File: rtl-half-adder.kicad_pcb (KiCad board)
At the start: 2 copper layers, 152.4 x 114.3 mm, 78 parts, among them Q1 Q_NPN_EBC, Q10 Q_NPN_EBC, Q11 Q_NPN_EBC, Q12 Q_NPN_EBC, Q13 Q_NPN_EBC, Q14 Q_NPN_BEC, Q15 Q_NPN_BEC, Q16 Q_NPN_EBC, Q17 Q_NPN_BEC, Q18 Q_NPN_BEC, Q19 Q_NPN_EBC, Q2 Q_NPN_EBC, Q3 Q_NPN_EBC, Q4 Q_NPN_EBC, Q5 Q_NPN_EBC, Q6 Q_NPN_EBC, Q7 Q_NPN_EBC, Q8 Q_NPN_EBC, Q9 Q_NPN_EBC, SW1 SW_DIP_x02

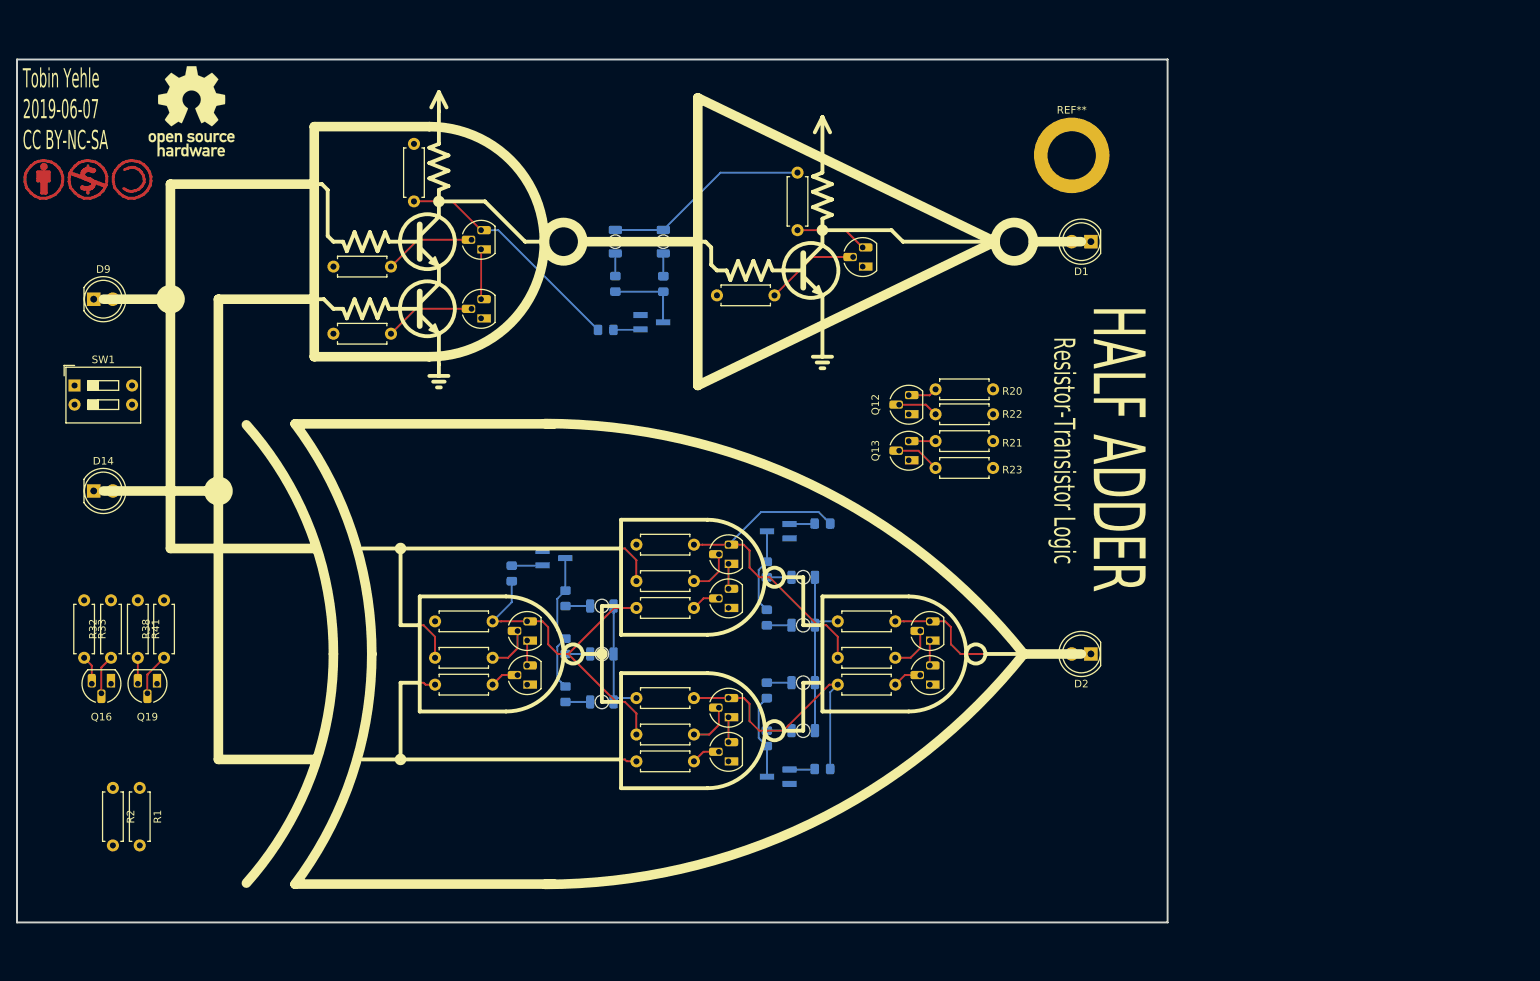
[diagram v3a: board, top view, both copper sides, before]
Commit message: refactor numeric assignments
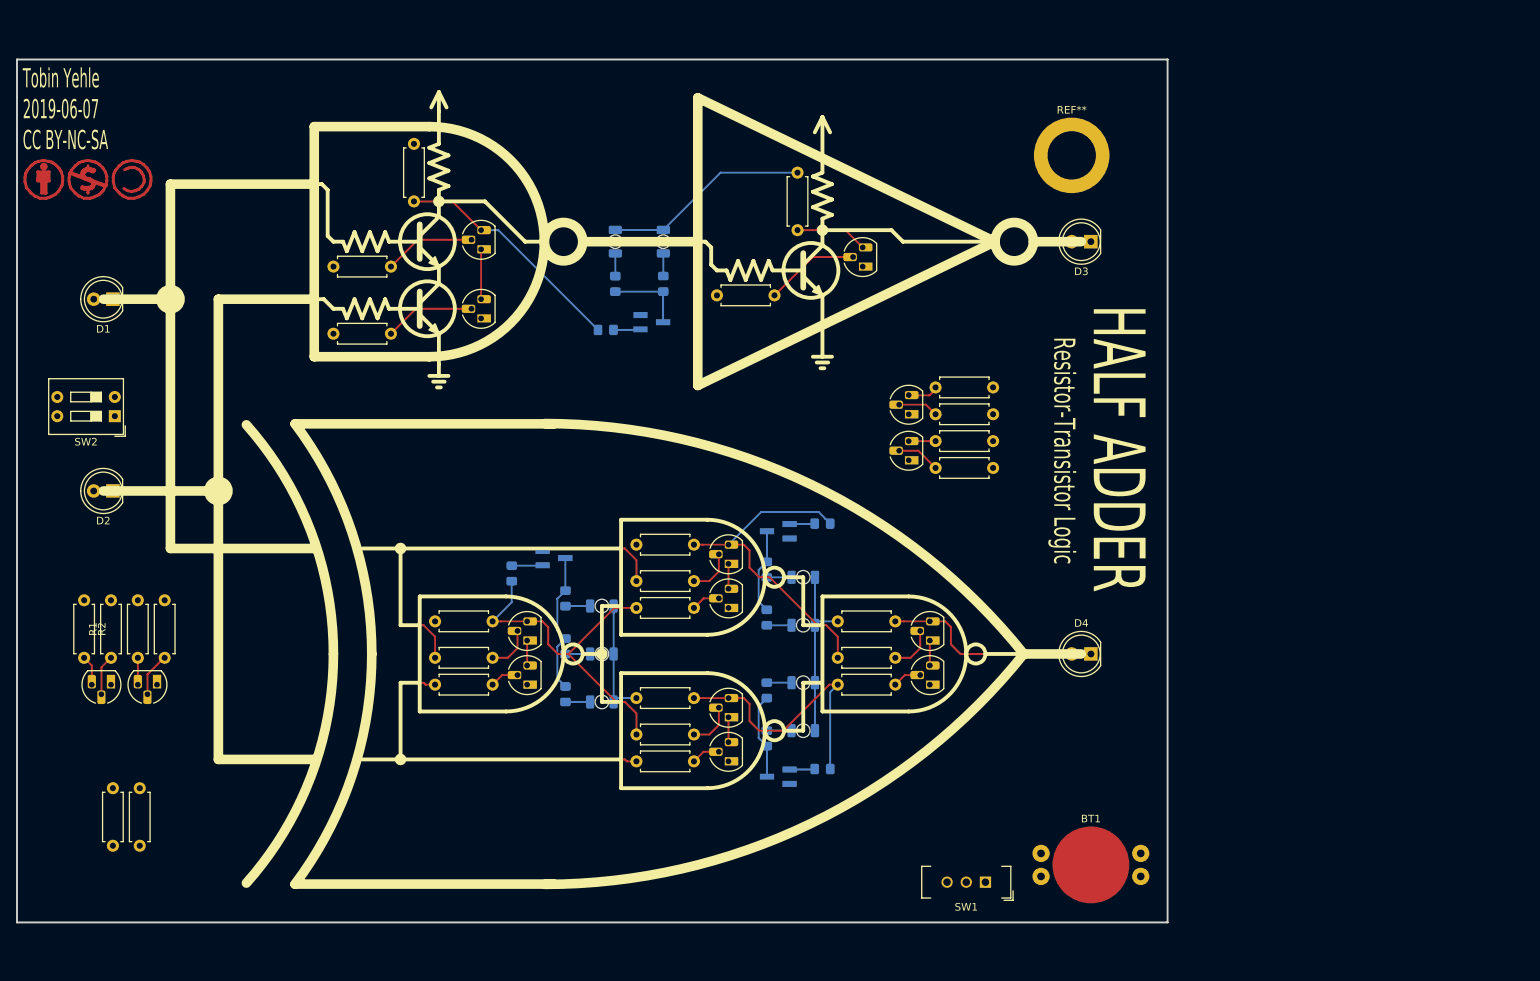
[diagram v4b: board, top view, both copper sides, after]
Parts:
- removed D14: LED, LED_THT:LED_D5.0mm
- removed D15: LED, --Project:LED_1206_3216Metric_ReverseMount_Hole1.8x2.4mm
- removed R41: 68, Resistor_THT:R_Axial_DIN0207_L6.3mm_D2.5mm_P7.62mm_Horizontal
- removed R42: 68, Resistor_SMD:R_0805_2012Metric_Pad1.15x1.40mm_HandSolder
- removed the REF** at (73.9, 45.0)
- added BT1: Battery_Cell, --Project:BatteryHolder_CR1220_THT, F.Cu at (193.0, 144.8)
- added D7: LED, --Project:LED_1206_3216Metric_ReverseMount_Hole1.8x2.4mm, B.Cu at (128.3, 110.5)
- added D8: LED, --Project:LED_1206_3216Metric_ReverseMount_Hole1.8x2.4mm, B.Cu at (128.3, 116.8)
- added R30: 68, Resistor_SMD:R_0805_2012Metric_Pad1.15x1.40mm_HandSolder, B.Cu at (136.4, 67.8)
- added R31: 10k, Resistor_SMD:R_0805_2012Metric_Pad1.15x1.40mm_HandSolder, B.Cu at (116.3, 106.2)
- added SW2: SW_DIP_x02, Button_Switch_THT:SW_DIP_SPSTx02_Slide_9.78x7.26mm_W7.62mm_P2.54mm, F.Cu at (63.8, 85.3)
- D3, D4: footprint --Project:LED_1206_3216Metric_ReverseMount_Hole1.8x2.4mm -> LED_THT:LED_D5.0mm; moved to F.Cu
- D9: footprint LED_THT:LED_D5.0mm -> --Project:LED_1206_3216Metric_ReverseMount_Hole1.8x2.4mm; moved to B.Cu
- Q14, Q15: value Q_NPN_BEC -> Q_NPN_EBC; footprint Package_TO_SOT_SMD:SOT-23_Handsoldering -> Package_TO_SOT_THT:TO-92_HandSolder; moved to F.Cu
- Q16, Q19: value Q_NPN_EBC -> Q_NPN_BEC; footprint Package_TO_SOT_THT:TO-92_HandSolder -> Package_TO_SOT_SMD:SOT-23_Handsoldering; moved to B.Cu
- R12, R17, R18, R23, R9: value 10k -> 1k
- R14, R15, R16, R19, R7, R8: value 1k -> 10k
- R2, R34, R4: value 10k -> 68
- R20: value 68 -> 1k
- R21, R28: value 68 -> 10k
- R24, R25, R26, R27: footprint Resistor_SMD:R_0805_2012Metric_Pad1.15x1.40mm_HandSolder -> Resistor_THT:R_Axial_DIN0207_L6.3mm_D2.5mm_P7.62mm_Horizontal; moved to F.Cu
- R32: value 10k -> 68; footprint Resistor_THT:R_Axial_DIN0207_L6.3mm_D2.5mm_P7.62mm_Horizontal -> Resistor_SMD:R_0805_2012Metric_Pad1.15x1.40mm_HandSolder; moved to B.Cu
- R33, R38: footprint Resistor_THT:R_Axial_DIN0207_L6.3mm_D2.5mm_P7.62mm_Horizontal -> Resistor_SMD:R_0805_2012Metric_Pad1.15x1.40mm_HandSolder; moved to B.Cu
- SW1: value SW_DIP_x02 -> SW_SPDT; footprint Button_Switch_THT:SW_DIP_SPSTx02_Slide_9.78x7.26mm_W7.62mm_P2.54mm -> --Project:SW_EG1218_SPDT
- moved SW1 135.2 mm to (176.5, 147.1), turned to 180 degrees
- moved D2 131.3 mm to (63.5, 95.2)
- moved D1 129.8 mm to (63.5, 69.8)
- moved R38 88.4 mm to (157.5, 132.1), turned to 0 degrees
- moved R12 86.6 mm to (103.4, 49.3), turned to 270 degrees
- moved Q16 86.2 mm to (134.9, 72.9), turned to 0 degrees
- moved D9 85.9 mm to (128.3, 123.2)
- moved Q19 83.2 mm to (151.6, 133.1)
- moved Q1 75.7 mm to (63.2, 120.9), turned to 180 degrees
- moved R7 68.9 mm to (113.8, 117.3), turned to 180 degrees
- moved Q2 64.8 mm to (69.3, 120.9), turned to 180 degrees
- moved R33 64.0 mm to (123.4, 115.8), turned to 90 degrees
- moved D3 63.0 mm to (193.0, 62.2), turned to 180 degrees
- moved R9 62.3 mm to (106.2, 112.5), turned to 0 degrees
- moved R32 60.7 mm to (123.4, 109.5)
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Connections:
- Q1 pad 1: Net-(Q1-Pad1) -> GND
- Q1 pad 3: NAND1 -> /A_GATE
- Q10 pad 1: Net-(Q10-Pad1) -> GND
- Q10 pad 3: SUM -> Net-(Q10-Pad3)
- Q11 pad 3: Net-(Q10-Pad1) -> CARRY
- Q12 pad 1: GND -> Net-(Q12-Pad1)
- Q12 pad 3: Net-(Q12-Pad3) -> SUM
- Q13 pad 3: Net-(Q13-Pad3) -> Net-(Q12-Pad1)
- Q14 pad 1: Net-(Q14-Pad1) -> GND
- Q14 pad 2: GND -> Net-(Q14-Pad2)
- Q14 pad 3: Net-(Q14-Pad3) -> /CARRY_GATE
- Q15 pad 1: Net-(Q15-Pad1) -> GND
- Q15 pad 2: GND -> Net-(Q15-Pad2)
- Q15 pad 3: Net-(Q15-Pad3) -> /SUM_GATE
- Q16 pad 1: GND -> Net-(Q16-Pad1)
- Q16 pad 2: Net-(Q16-Pad2) -> GND
- Q19 pad 1: GND -> Net-(Q19-Pad1)
- Q19 pad 2: Net-(Q19-Pad2) -> GND
- Q2 pad 3: Net-(Q1-Pad1) -> /B_GATE
- Q5 pad 1: GND -> Net-(Q5-Pad1)
- Q5 pad 3: CARRY -> NAND1
- Q6 pad 1: Net-(Q6-Pad1) -> GND
- Q6 pad 3: XOR2 -> Net-(Q5-Pad1)
- Q7 pad 1: GND -> Net-(Q7-Pad1)
- Q7 pad 3: Net-(Q6-Pad1) -> XOR2
- Q8 pad 1: Net-(Q8-Pad1) -> GND
- Q8 pad 3: XOR3 -> Net-(Q7-Pad1)
- Q9 pad 1: GND -> Net-(Q10-Pad3)
- Q9 pad 3: Net-(Q8-Pad1) -> XOR3
- R1 pad 1: B -> Net-(Q1-Pad2)
- R1 pad 2: GND -> A
- R10 pad 1: Net-(Q6-Pad2) -> Net-(Q5-Pad2)
- R11 pad 1: Net-(Q7-Pad2) -> Net-(Q6-Pad2)
- R11 pad 2: XOR1 -> B
- R12 pad 1: Net-(Q8-Pad2) -> VCC
- R12 pad 2: XOR1 -> NAND1
- R13 pad 1: Net-(Q9-Pad2) -> Net-(Q7-Pad2)
- R13 pad 2: B -> A
- R14 pad 1: VCC -> Net-(Q8-Pad2)
- R14 pad 2: CARRY -> XOR1
- R15 pad 1: VCC -> Net-(Q9-Pad2)
- R15 pad 2: XOR2 -> XOR1
- R16 pad 1: VCC -> Net-(Q10-Pad2)
- R16 pad 2: XOR3 -> B
- R17 pad 1: Net-(Q10-Pad2) -> VCC
- R18 pad 1: Net-(Q11-Pad2) -> VCC
- R19 pad 1: VCC -> Net-(Q11-Pad2)
- R19 pad 2: SUM -> NAND1
- R2 pad 1: A -> Net-(D1-Pad1)
- R2 pad 2: GND -> /A_GATE
- R20 pad 1: Net-(D1-Pad1) -> VCC
- R20 pad 2: Net-(Q12-Pad3) -> CARRY
- R21 pad 1: Net-(D2-Pad1) -> Net-(Q12-Pad2)
- R21 pad 2: Net-(Q13-Pad3) -> XOR2
- R22 pad 1: Net-(Q12-Pad2) -> Net-(Q13-Pad2)
- R22 pad 2: CARRY -> XOR3
- R23 pad 1: Net-(Q13-Pad2) -> VCC
- R24 pad 1: Net-(Q14-Pad1) -> Net-(Q14-Pad2)
- R24 pad 2: NAND1 -> CARRY
- R25 pad 1: Net-(Q15-Pad1) -> Net-(Q15-Pad2)
- R25 pad 2: XOR2 -> SUM
- R26 pad 2: Net-(Q14-Pad3) -> /CARRY_GATE
- R27 pad 2: Net-(Q15-Pad3) -> /SUM_GATE
- R28 pad 1: Net-(D5-Pad1) -> Net-(Q16-Pad1)
- R28 pad 2: Net-(Q14-Pad3) -> NAND1
- R29 pad 1: Net-(D6-Pad1) -> Net-(D5-Pad1)
- R29 pad 2: Net-(Q15-Pad3) -> Net-(Q16-Pad3)
- R3 pad 1: Net-(Q1-Pad2) -> Net-(Q2-Pad2)
- R3 pad 2: A -> B
- R32 pad 1: Net-(Q16-Pad2) -> Net-(D7-Pad1)
- R32 pad 2: A -> Net-(Q17-Pad3)
- R33 pad 1: Net-(D9-Pad1) -> Net-(D8-Pad1)
- R33 pad 2: Net-(Q16-Pad3) -> Net-(Q17-Pad3)
- R34 pad 1: Net-(Q17-Pad1) -> Net-(D9-Pad1)
- R34 pad 2: XOR1 -> Net-(Q17-Pad3)
- R35 pad 2: XOR3 -> XOR2
- R36 pad 2: Net-(Q17-Pad3) -> Net-(Q18-Pad3)
- R38 pad 1: Net-(Q19-Pad2) -> Net-(Q19-Pad1)
- R38 pad 2: B -> XOR3
- R39 pad 2: Net-(Q17-Pad3) -> Net-(Q19-Pad3)
- R4 pad 1: Net-(Q2-Pad2) -> Net-(D2-Pad1)
- R4 pad 2: B -> /B_GATE
- R40 pad 2: Net-(Q18-Pad3) -> Net-(Q19-Pad3)
- R5 pad 1: Net-(Q3-Pad2) -> B
- R5 pad 2: A -> GND
- R6 pad 1: Net-(Q4-Pad2) -> A
- R6 pad 2: B -> GND
- R7 pad 1: VCC -> Net-(Q3-Pad2)
- R7 pad 2: NAND1 -> A
- R8 pad 1: VCC -> Net-(Q4-Pad2)
- R8 pad 2: XOR1 -> B
- R9 pad 1: Net-(Q5-Pad2) -> VCC
- R9 pad 2: NAND1 -> XOR1
- SW1 pad 1: VCC -> Net-(BT1-Pad1)
- SW1 pad 3: B -> (no net)
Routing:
- net Net-(Q15-Pad3): track 11.3 -> 0.00 mm
- net Net-(Q14-Pad3): track 10.4 -> 0.00 mm
- net Net-(Q11-Pad2): track 3.83 -> 12.5 mm
- net Net-(Q19-Pad3): track 3.43 -> 11.3 mm
- net Net-(Q1-Pad2): track 12.1 -> 5.35 mm
- net Net-(Q5-Pad1): track 0.00 -> 6.60 mm
- net Net-(Q1-Pad1): track 6.60 -> 0.00 mm
- net Net-(Q16-Pad3): track 3.85 -> 10.4 mm
- net Net-(Q2-Pad2): track 12.0 -> 5.61 mm
- net Net-(Q6-Pad2): track 6.11 -> 12.0 mm
- net Net-(Q15-Pad2): track 0.00 -> 5.77 mm
- net Net-(Q19-Pad2): track 5.61 -> 0.00 mm
- net Net-(Q14-Pad2): track 0.00 -> 5.35 mm
- net Net-(Q16-Pad2): track 5.23 -> 0.00 mm
- net Net-(Q12-Pad3): track 3.90 -> 0.00 mm
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
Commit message: fix front fab layer
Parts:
- added SW3: SW_SPDT, --Project:SW_EG1218_SPDT, F.Cu at (61.0, 85.9)
- REF**: value MountingHole_6.4mm_M6_ISO14580_Pad -> MountingHole_6.4mm
- SW2: value SW_DIP_x02 -> SW_SPDT; footprint Button_Switch_THT:SW_DIP_SPSTx02_Slide_9.78x7.26mm_W7.62mm_P2.54mm -> --Project:SW_EG1218_SPDT
- moved SW2 6.71 mm to (61.0, 79.2)
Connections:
- SW1 pad 3: (no net) -> Net-(SW1-Pad3)
- SW2 pad 1: VCC -> A
- SW2 pad 3: B -> Net-(SW2-Pad3)
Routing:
- net VCC: track 66.8 -> 391.5 mm
- net A: track 41.1 -> 212.0 mm, vias 0 -> 2
- net B: track 34.5 -> 159.2 mm
- net Net-(D1-Pad1): track 0.00 -> 47.8 mm
- net Net-(BT1-Pad1): track 0.00 -> 40.2 mm
- net NAND1: track 31.4 -> 66.2 mm
- net CARRY: track 9.58 -> 44.2 mm
- net Net-(D4-Pad1): track 0.00 -> 33.6 mm
- net Net-(D3-Pad1): track 0.00 -> 24.7 mm
- net Net-(D2-Pad1): track 0.00 -> 15.8 mm
- net SUM: track 21.4 -> 30.3 mm
- added copper zone on B.Cu, net GND
- added copper zone on F.Cu, net GND

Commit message: put notes on the back
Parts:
- added REF**: OSHW-Logo_11.4x12mm_SilkScreen, Symbol:OSHW-Logo_11.4x12mm_SilkScreen, B.Cu at (139.4, 46.0)
- REF** (x3): moved to B.Cu
- moved REF** 109.4 mm to (163.6, 47.9), turned to 180 degrees
- moved REF** 97.7 mm to (157.7, 47.9), turned to 180 degrees
- moved REF** 86.1 mm to (151.9, 47.9), turned to 180 degrees
- moved D3 4.06 mm to (197.1, 62.2)
- moved D4 4.06 mm to (197.1, 116.8)
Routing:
- net VCC: track 391.5 -> 400.2 mm
- net Net-(D4-Pad1): track 33.6 -> 35.6 mm
- net Net-(D3-Pad1): track 24.7 -> 26.7 mm
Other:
- board text added: "CC BY-NC-SA"
- board text added: "Tobin Yehle 2019-06-11 v1"
- board text removed: "Tobin Yehle 2019-06-07 CC BY-NC-SA"
